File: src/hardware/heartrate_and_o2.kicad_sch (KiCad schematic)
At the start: 9 parts, among them J52 Conn_01x02_Pin, J53 Conn_01x02_Pin, J54 Conn_01x01_Pin, J55 Conn_01x02_Pin, U17 MAX30101EFD_T

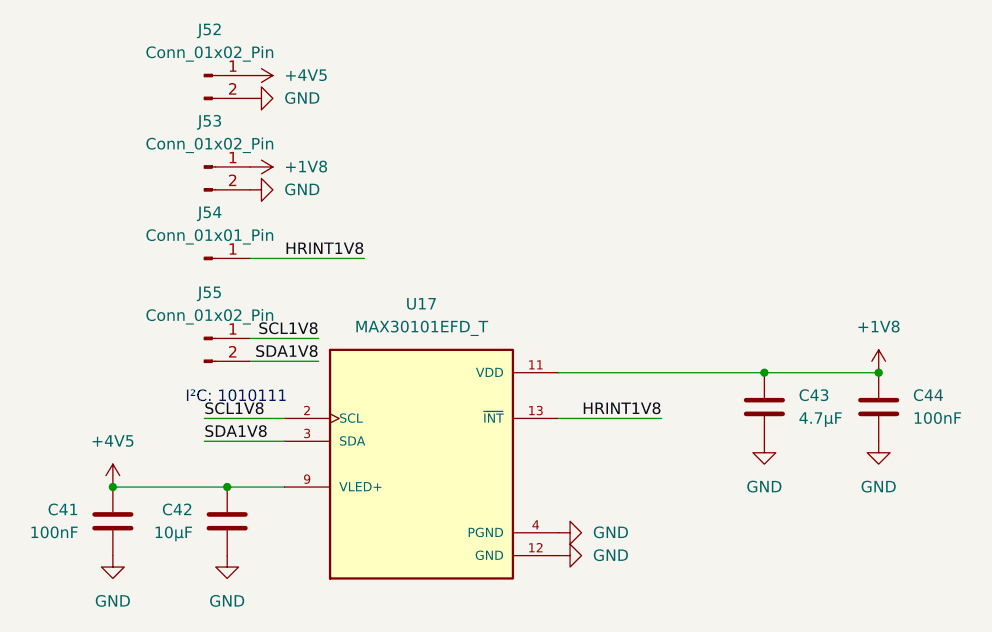
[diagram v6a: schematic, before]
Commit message: Fixed symbol of MAX30101EFD_T
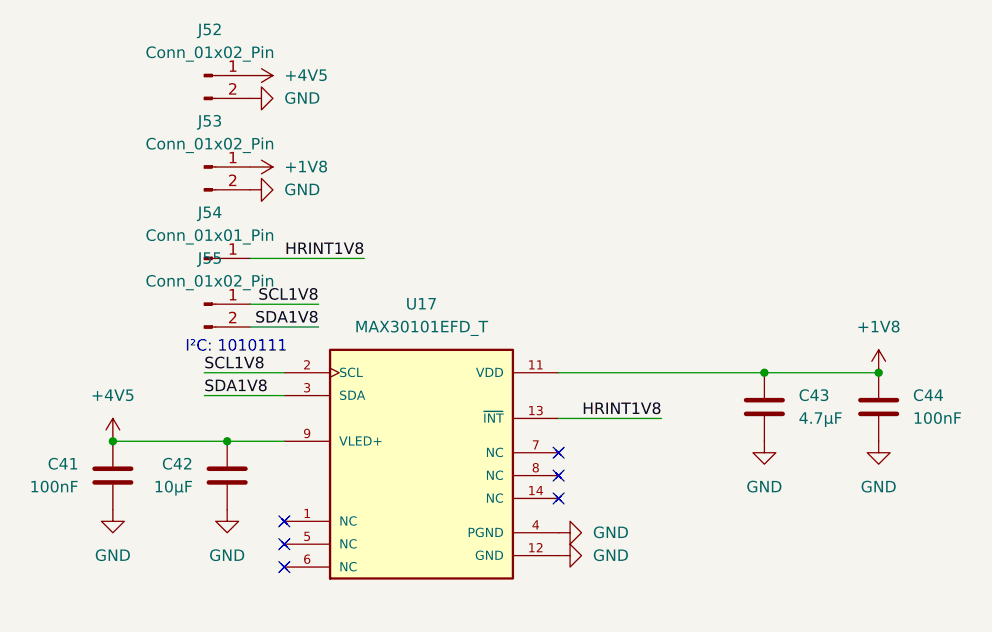
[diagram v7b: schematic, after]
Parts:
- U17: footprint Project:PSON80P560X330X165-14N -> MAX30101EFD_T:PSON80P560X330X165-14N
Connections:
- net +4V5: no longer U17.10 (VLED+)
- no-connect marks 0 -> 6
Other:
- moved on the sheet: C41, C42, J55
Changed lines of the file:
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@@
 	(text "I²C: 1010111"
 		(exclude_from_sim no)
-		(at 126.746 89.154 0)
+		(at 126.746 83.566 0)
 		(effects
 			(font
@@
 	)
 	(junction
-		(at 125.73 99.06)
-		(diameter 0)
-		(color 0 0 0 0)
-	)
-	(junction
 		(at 198.12 86.36)
 		(diameter 0)
@@
 	)
 	(junction
-		(at 113.03 99.06)
+		(at 113.03 93.98)
 		(diameter 0)
 		(color 0 0 0 0)
 	)
+	(junction
+		(at 125.73 93.98)
+		(diameter 0)
+		(color 0 0 0 0)
+	)
+	(no_connect
+		(at 132.08 105.41)
+	)
+	(no_connect
+		(at 132.08 102.87)
+	)
+	(no_connect
+		(at 162.56 95.25)
+	)
+	(no_connect
+		(at 162.56 100.33)
+	)
+	(no_connect
+		(at 162.56 97.79)
+	)
+	(no_connect
+		(at 132.08 107.95)
+	)
 	(wire
 		(pts
-			(xy 125.73 99.06) (xy 132.08 99.06)
+			(xy 125.73 93.98) (xy 132.08 93.98)
 		)
 		(stroke
@@
 	(wire
 		(pts
-			(xy 123.19 93.98) (xy 132.08 93.98)
+			(xy 123.19 88.9) (xy 132.08 88.9)
 		)
 		(stroke
@@
 	(wire
 		(pts
-			(xy 135.89 82.55) (xy 128.27 82.55)
+			(xy 135.89 78.74) (xy 128.27 78.74)
 		)
 		(stroke
@@
 	(wire
 		(pts
-			(xy 123.19 91.44) (xy 132.08 91.44)
+			(xy 123.19 86.36) (xy 132.08 86.36)
 		)
 		(stroke
@@
 	(wire
 		(pts
-			(xy 135.89 85.09) (xy 128.27 85.09)
+			(xy 135.89 81.28) (xy 128.27 81.28)
 		)
 		(stroke
@@
 	(wire
 		(pts
-			(xy 113.03 99.06) (xy 125.73 99.06)
+			(xy 113.03 93.98) (xy 125.73 93.98)
 		)
 		(stroke
@@
 	)
 	(label "SDA1V8"
-		(at 123.19 93.98 0)
+		(at 123.19 88.9 0)
 		(effects
 			(font
@@
 	)
 	(label "SDA1V8"
-		(at 135.89 85.09 180)
+		(at 135.89 81.28 180)
 		(effects
 			(font
@@
 	)
 	(label "SCL1V8"
-		(at 135.89 82.55 180)
+		(at 135.89 78.74 180)
 		(effects
 			(font
@@
 	)
 	(label "SCL1V8"
-		(at 123.19 91.44 0)
+		(at 123.19 86.36 0)
 		(effects
 			(font
@@
 	(symbol
 		(lib_id "Device:C")
-		(at 113.03 102.87 0)
+		(at 113.03 97.79 0)
 		(mirror y)
 		(unit 1)
@@
 		(fields_autoplaced yes)
 		(property "Reference" "C41"
-			(at 109.22 101.5999 0)
+			(at 109.22 96.5199 0)
 			(effects
 				(font
@@
 		)
 		(property "Value" "100nF"
-			(at 109.22 104.1399 0)
+			(at 109.22 99.0599 0)
 			(effects
 				(font
@@
 		)
 		(property "Footprint" "Capacitor_SMD:C_0504_1310Metric"
-			(at 112.0648 106.68 0)
+			(at 112.0648 101.6 0)
 			(effects
 				(font
@@
 		)
 		(property "Datasheet" "~"
-			(at 113.03 102.87 0)
+			(at 113.03 97.79 0)
 			(effects
 				(font
@@
 		)
 		(property "Description" "Unpolarized capacitor"
-			(at 113.03 102.87 0)
+			(at 113.03 97.79 0)
 			(effects
 				(font
@@
 		)
 		(property "β(25/85)" ""
-			(at 113.03 102.87 0)
+			(at 113.03 97.79 0)
 			(effects
 				(font
@@
 	(symbol
 		(lib_id "Connector:Conn_01x02_Pin")
-		(at 123.19 82.55 0)
+		(at 123.19 78.74 0)
 		(unit 1)
 		(exclude_from_sim no)
@@
 		(fields_autoplaced yes)
 		(property "Reference" "J55"
-			(at 123.825 77.47 0)
+			(at 123.825 73.66 0)
 			(effects
 				(font
@@
 		)
 		(property "Value" "Conn_01x02_Pin"
-			(at 123.825 80.01 0)
+			(at 123.825 76.2 0)
 			(effects
 				(font
@@
 		)
 		(property "Footprint" "Connector_PinHeader_2.54mm:PinHeader_1x02_P2.54mm_Horizontal"
-			(at 123.19 82.55 0)
+			(at 123.19 78.74 0)
 			(effects
 				(font
@@
 		)
 		(property "Datasheet" "~"
-			(at 123.19 82.55 0)
+			(at 123.19 78.74 0)
 			(effects
 				(font
@@
 		)
 		(property "Description" "Generic connector, single row, 01x02, script generated"
-			(at 123.19 82.55 0)
+			(at 123.19 78.74 0)
 			(effects
 				(font
@@
 	(symbol
 		(lib_id "power:GND")
-		(at 125.73 106.68 0)
+		(at 125.73 101.6 0)
 		(mirror y)
 		(unit 1)
@@
 		(fields_autoplaced yes)
 		(property "Reference" "#PWR0308"
-			(at 125.73 113.03 0)
+			(at 125.73 107.95 0)
 			(effects
 				(font
@@
 		)
 		(property "Value" "GND"
-			(at 125.73 111.76 0)
+			(at 125.73 106.68 0)
 			(effects
 				(font
@@
 		)
 		(property "Footprint" ""
-			(at 125.73 106.68 0)
+			(at 125.73 101.6 0)
 			(effects
 				(font
@@
 		)
 		(property "Datasheet" ""
-			(at 125.73 106.68 0)
+			(at 125.73 101.6 0)
 			(effects
 				(font
@@
 		)
 		(property "Description" "Power symbol creates a global label with name \"GND\" , ground"
-			(at 125.73 106.68 0)
+			(at 125.73 101.6 0)
 			(effects
 				(font
@@
 	(symbol
 		(lib_id "power:+3V3")
-		(at 113.03 99.06 0)
+		(at 113.03 93.98 0)
 		(mirror y)
 		(unit 1)
@@
 		(fields_autoplaced yes)
 		(property "Reference" "#PWR0306"
-			(at 113.03 102.87 0)
+			(at 113.03 97.79 0)
 			(effects
 				(font
@@
 		)
 		(property "Value" "+4V5"
+			(at 113.03 88.9 0)
+			(effects
+				(font
+					(size 1.27 1.27)
+				)
+			)
+		)
+		(property "Footprint" ""
 			(at 113.03 93.98 0)
 			(effects
@@
 					(size 1.27 1.27)
 				)
-			)
-		)
-		(property "Footprint" ""
-			(at 113.03 99.06 0)
-			(effects
-				(font
-					(size 1.27 1.27)
-				)
 				(hide yes)
 			)
 		)
 		(property "Datasheet" ""
-			(at 113.03 99.06 0)
+			(at 113.03 93.98 0)
 			(effects
 				(font
@@
 		)
 		(property "Description" "Power symbol creates a global label with name \"+3V3\""
-			(at 113.03 99.06 0)
+			(at 113.03 93.98 0)
 			(effects
 				(font
@@
 	(symbol
 		(lib_id "Device:C")
-		(at 125.73 102.87 0)
+		(at 125.73 97.79 0)
 		(mirror y)
 		(unit 1)
@@
 		(fields_autoplaced yes)
 		(property "Reference" "C42"
-			(at 121.92 101.5999 0)
+			(at 121.92 96.5199 0)
 			(effects
 				(font
@@
 		)
 		(property "Value" "10µF"
-			(at 121.92 104.1399 0)
+			(at 121.92 99.0599 0)
 			(effects
 				(font
@@
 		)
 		(property "Footprint" "Capacitor_SMD:C_0504_1310Metric"
-			(at 124.7648 106.68 0)
+			(at 124.7648 101.6 0)
 			(effects
 				(font
@@
 		)
 		(property "Datasheet" "~"
-			(at 125.73 102.87 0)
+			(at 125.73 97.79 0)
 			(effects
 				(font
@@
 		)
 		(property "Description" "Unpolarized capacitor"
-			(at 125.73 102.87 0)
+			(at 125.73 97.79 0)
 			(effects
 				(font
@@
 		)
 		(property "β(25/85)" ""
-			(at 125.73 102.87 0)
+			(at 125.73 97.79 0)
 			(effects
 				(font
@@
 			)
 		)
-		(property "Footprint" "Project:PSON80P560X330X165-14N"
+		(property "Footprint" "MAX30101EFD_T:PSON80P560X330X165-14N"
 			(at 147.32 96.52 0)
 			(effects
@@
 		)
 		(pin "4"
+		)
+		(pin "6"
+		)
+		(pin "8"
+		)
+		(pin "5"
+		)
+		(pin "1"
+		)
+		(pin "14"
+		)
+		(pin "7"
 		)
 		(instances
@@
 	(symbol
 		(lib_id "power:GND")
-		(at 113.03 106.68 0)
+		(at 113.03 101.6 0)
 		(mirror y)
 		(unit 1)
@@
 		(fields_autoplaced yes)
 		(property "Reference" "#PWR0307"
-			(at 113.03 113.03 0)
+			(at 113.03 107.95 0)
 			(effects
 				(font
@@
 		)
 		(property "Value" "GND"
-			(at 113.03 111.76 0)
+			(at 113.03 106.68 0)
 			(effects
 				(font
@@
 		)
 		(property "Footprint" ""
-			(at 113.03 106.68 0)
+			(at 113.03 101.6 0)
 			(effects
 				(font
@@
 		)
 		(property "Datasheet" ""
-			(at 113.03 106.68 0)
+			(at 113.03 101.6 0)
 			(effects
 				(font
@@
 		)
 		(property "Description" "Power symbol creates a global label with name \"GND\" , ground"
-			(at 113.03 106.68 0)
-			(effects
-				(font
+			(at 113.03 101.6 0)
+			(effects
+				(font

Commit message: Reannotate
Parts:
- renumbered U17 to U16
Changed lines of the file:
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@@
 		(dnp no)
 		(fields_autoplaced yes)
-		(property "Reference" "#PWR0310"
+		(property "Reference" "#PWR0311"
 			(at 134.62 55.88 0)
 			(effects
@@
 			(project "raywatch"
 				(path "/7b654ee8-2a53-4d39-8b7d-32c7bb3cb0ed/92973ecd-838d-4692-844f-05a1efeb365a"
-					(reference "#PWR0310")
+					(reference "#PWR0311")
 					(unit 1)
 				)
@@
 		(dnp no)
 		(fields_autoplaced yes)
-		(property "Reference" "#PWR0316"
+		(property "Reference" "#PWR0317"
 			(at 198.12 90.17 0)
 			(effects
@@
 			(project "raywatch"
 				(path "/7b654ee8-2a53-4d39-8b7d-32c7bb3cb0ed/92973ecd-838d-4692-844f-05a1efeb365a"
-					(reference "#PWR0316")
+					(reference "#PWR0317")
 					(unit 1)
 				)
@@
 		(dnp no)
 		(fields_autoplaced yes)
-		(property "Reference" "#PWR0308"
+		(property "Reference" "#PWR0309"
 			(at 125.73 107.95 0)
 			(effects
@@
 			(project "raywatch"
 				(path "/7b654ee8-2a53-4d39-8b7d-32c7bb3cb0ed/92973ecd-838d-4692-844f-05a1efeb365a"
-					(reference "#PWR0308")
+					(reference "#PWR0309")
 					(unit 1)
 				)
@@
 		(dnp no)
 		(fields_autoplaced yes)
-		(property "Reference" "#PWR0309"
+		(property "Reference" "#PWR0310"
 			(at 124.46 53.34 0)
 			(effects
@@
 			(project "raywatch"
 				(path "/7b654ee8-2a53-4d39-8b7d-32c7bb3cb0ed/92973ecd-838d-4692-844f-05a1efeb365a"
-					(reference "#PWR0309")
+					(reference "#PWR0310")
 					(unit 1)
 				)
@@
 		(dnp no)
 		(fields_autoplaced yes)
-		(property "Reference" "#PWR0315"
+		(property "Reference" "#PWR0316"
 			(at 185.42 100.33 0)
 			(effects
@@
 			(project "raywatch"
 				(path "/7b654ee8-2a53-4d39-8b7d-32c7bb3cb0ed/92973ecd-838d-4692-844f-05a1efeb365a"
-					(reference "#PWR0315")
+					(reference "#PWR0316")
 					(unit 1)
 				)
@@
 		(dnp no)
 		(fields_autoplaced yes)
-		(property "Reference" "#PWR0306"
+		(property "Reference" "#PWR0307"
 			(at 113.03 97.79 0)
 			(effects
@@
 			(project "raywatch"
 				(path "/7b654ee8-2a53-4d39-8b7d-32c7bb3cb0ed/92973ecd-838d-4692-844f-05a1efeb365a"
-					(reference "#PWR0306")
+					(reference "#PWR0307")
 					(unit 1)
 				)
@@
 		(dnp no)
 		(fields_autoplaced yes)
-		(property "Reference" "#PWR0312"
+		(property "Reference" "#PWR0313"
 			(at 134.62 66.04 0)
 			(effects
@@
 			(project "raywatch"
 				(path "/7b654ee8-2a53-4d39-8b7d-32c7bb3cb0ed/92973ecd-838d-4692-844f-05a1efeb365a"
-					(reference "#PWR0312")
+					(reference "#PWR0313")
 					(unit 1)
 				)
@@
 		(dnp no)
 		(fields_autoplaced yes)
-		(property "Reference" "#PWR0311"
+		(property "Reference" "#PWR0312"
 			(at 124.46 63.5 0)
 			(effects
@@
 			(project "raywatch"
 				(path "/7b654ee8-2a53-4d39-8b7d-32c7bb3cb0ed/92973ecd-838d-4692-844f-05a1efeb365a"
-					(reference "#PWR0311")
+					(reference "#PWR0312")
 					(unit 1)
 				)
@@
 		(dnp no)
 		(fields_autoplaced yes)
-		(property "Reference" "#PWR0313"
+		(property "Reference" "#PWR0314"
 			(at 168.91 104.14 0)
 			(effects
@@
 			(project "raywatch"
 				(path "/7b654ee8-2a53-4d39-8b7d-32c7bb3cb0ed/92973ecd-838d-4692-844f-05a1efeb365a"
-					(reference "#PWR0313")
+					(reference "#PWR0314")
 					(unit 1)
 				)
@@
 		(dnp no)
 		(fields_autoplaced yes)
-		(property "Reference" "U17"
+		(property "Reference" "U16"
 			(at 147.32 78.74 0)
 			(effects
@@
 			(project "raywatch"
 				(path "/7b654ee8-2a53-4d39-8b7d-32c7bb3cb0ed/92973ecd-838d-4692-844f-05a1efeb365a"
-					(reference "U17")
+					(reference "U16")
 					(unit 1)
 				)
@@
 		(dnp no)
 		(fields_autoplaced yes)
-		(property "Reference" "#PWR0317"
+		(property "Reference" "#PWR0318"
 			(at 198.12 100.33 0)
 			(effects
@@
 			(project "raywatch"
 				(path "/7b654ee8-2a53-4d39-8b7d-32c7bb3cb0ed/92973ecd-838d-4692-844f-05a1efeb365a"
-					(reference "#PWR0317")
+					(reference "#PWR0318")
 					(unit 1)
 				)
@@
 		(dnp no)
 		(fields_autoplaced yes)
-		(property "Reference" "#PWR0314"
+		(property "Reference" "#PWR0315"
 			(at 168.91 106.68 0)
 			(effects
@@
 			(project "raywatch"
 				(path "/7b654ee8-2a53-4d39-8b7d-32c7bb3cb0ed/92973ecd-838d-4692-844f-05a1efeb365a"
-					(reference "#PWR0314")
+					(reference "#PWR0315")
 					(unit 1)
 				)
@@
 		(dnp no)
 		(fields_autoplaced yes)
-		(property "Reference" "#PWR0307"
+		(property "Reference" "#PWR0308"
 			(at 113.03 107.95 0)
 			(effects
@@
 			(project "raywatch"
 				(path "/7b654ee8-2a53-4d39-8b7d-32c7bb3cb0ed/92973ecd-838d-4692-844f-05a1efeb365a"
-					(reference "#PWR0307")
-					(unit 1)
-				)
+					(reference "#PWR0308")
+					(unit 1)
+				)
